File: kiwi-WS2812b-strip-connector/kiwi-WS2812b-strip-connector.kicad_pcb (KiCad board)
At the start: 2 copper layers, 41.7 x 12.3 mm, 12 parts, among them J1 Conn_01x03, J2 Conn_01x03, SW1 SW_Push, U2 WS2812B_fromStrip, U4 WS2812B_fromStrip, U5 WS2812B_toStrip, U7 WS2812B_toStrip

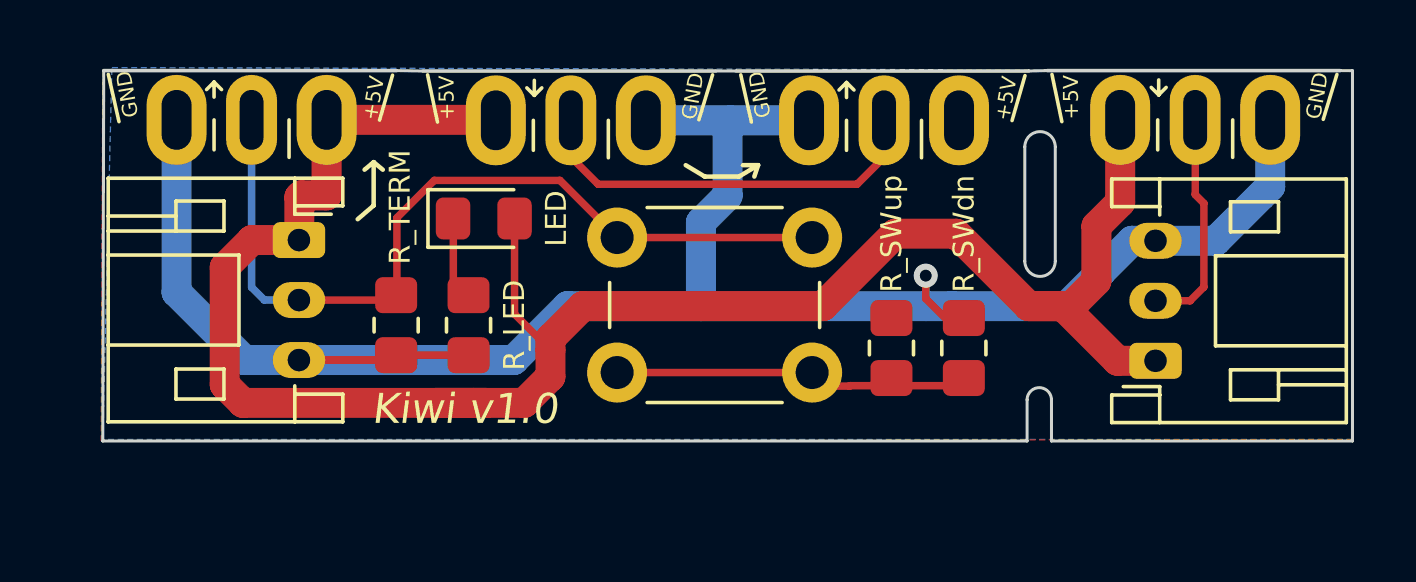
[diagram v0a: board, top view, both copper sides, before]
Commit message: Added USB connector as alternate footprint
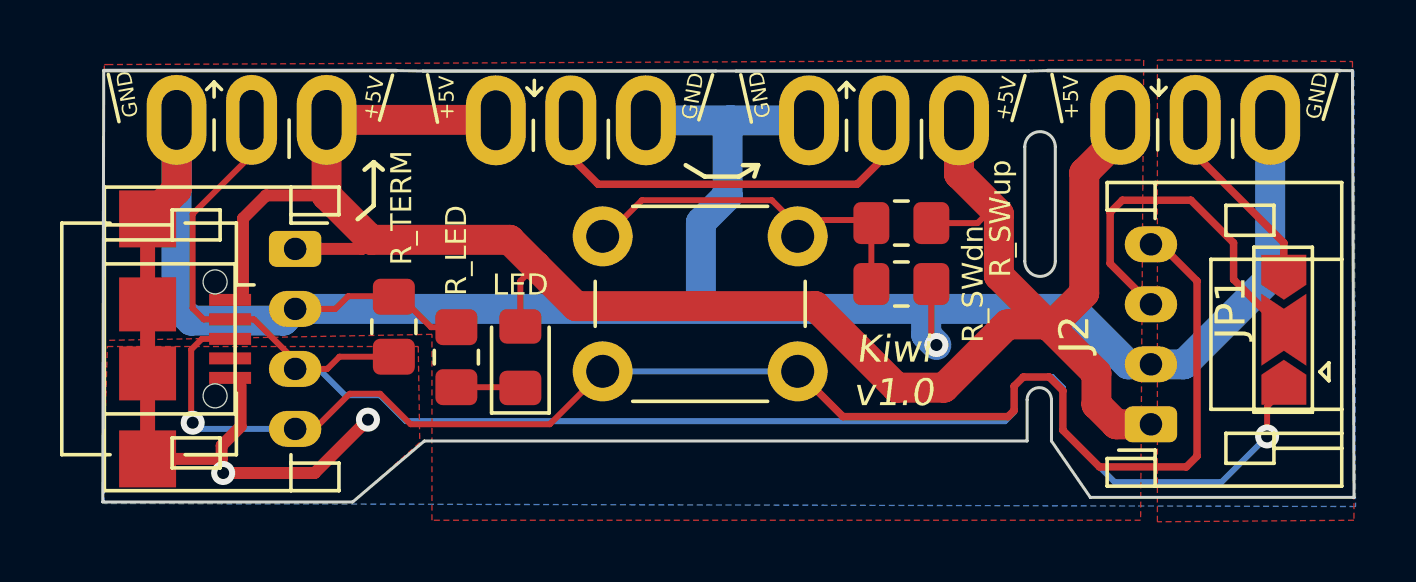
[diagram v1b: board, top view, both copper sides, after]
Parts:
- added J3: USB_B_Micro, Connector_USB_Extra:USB_Micro_MIUSB-F5M-BB-U, F.Cu at (109.7, 75.4)
- added JP1: SolderJumper_3_Open, Jumper:SolderJumper-3_P2.0mm_Open_TrianglePad1.0x1.5mm, F.Cu at (146.3, 75.1)
- J1, J2: value Conn_01x03 -> Conn_01x04; footprint Connector_JST:JST_PH_S3B-PH-K_1x03_P2.00mm_Horizontal -> Connector_JST:JST_PH_S4B-PH-K_1x04_P2.00mm_Horizontal
- moved SW1 7.49 mm to (130.1, 76.5), turned to 180 degrees
- moved D1 4.78 mm to (120.9, 76.0), turned to 90 degrees
- moved R4 4.18 mm to (133.6, 71.5), turned to 180 degrees
- moved R1 2.98 mm to (133.6, 73.6), turned to 0 degrees
- moved J2 2.12 mm to (141.9, 78.2)
- moved R3 1.14 mm to (118.7, 76.0), turned to 90 degrees
- moved J1 0.32 mm to (113.3, 72.4)
- moved R2 0.09 mm to (116.6, 75.0), turned to 90 degrees
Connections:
- J1 pad 2: /DATA_IN -> GND
- J1 pad 3: GND -> /DATA_IN
- J2 pad 2: /DATA_OUT -> GND
- J2 pad 3: GND -> Net-(J2-Pad3)
- SW1 pad 1: /DATA_IN -> /MISC_IO
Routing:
- net /MISC_IO: track 0.00 -> 49.8 mm, vias 0 -> 1
- net /DATA_IN: track 28.2 -> 52.5 mm, vias 0 -> 1
- net GND: track 70.7 -> 94.5 mm, vias 1 -> 3
- net Net-(J2-Pad3): track 0.00 -> 12.1 mm
- net /DATA_OUT: track 7.49 -> 5.08 mm
- net +5V: track 68.2 -> 69.4 mm
- added copper zone on F.Cu, net GND
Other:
- board size 41.7 x 12.3 mm -> 41.7 x 14.4 mm

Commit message: Commented schematics and updated PCB, both pass DRC
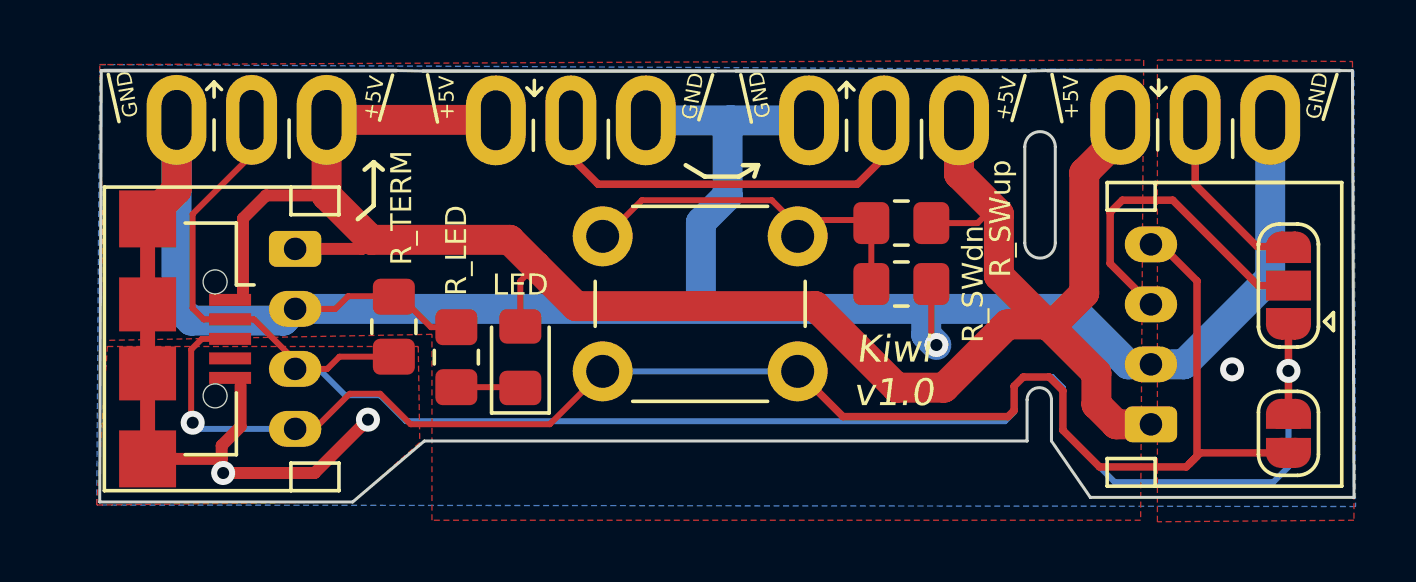
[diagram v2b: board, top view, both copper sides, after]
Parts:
- added JP2: misc_to_data, Jumper:SolderJumper-2_P1.3mm_Open_RoundedPad1.0x1.5mm, F.Cu at (146.5, 78.5)
- JP1: value SolderJumper_3_Open -> data_in_vs_out; footprint Jumper:SolderJumper-3_P2.0mm_Open_TrianglePad1.0x1.5mm -> Jumper:SolderJumper-3_P1.3mm_Open_RoundedPad1.0x1.5mm
- moved JP1 1.48 mm to (146.5, 73.6)
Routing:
- net /DATA_IN: track 52.5 -> 57.1 mm
- net /MISC_IO: track 49.8 -> 53.3 mm
- net Net-(J2-Pad3): track 12.1 -> 10.9 mm
- net /DATA_OUT: track 5.08 -> 6.12 mm
- net GND: vias 3 -> 4
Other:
- board size 41.7 x 14.4 mm -> 41.8 x 14.4 mm
